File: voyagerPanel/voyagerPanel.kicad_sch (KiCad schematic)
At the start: 22 parts, among them J1 USB_C_Receptacle_USB2.0_16P, J2 Conn_01x02_Pin, U1 ESP32-S3-MINI-1, U2 MCP1700x-330xxMB, U4 TP4056-42-ESOP8

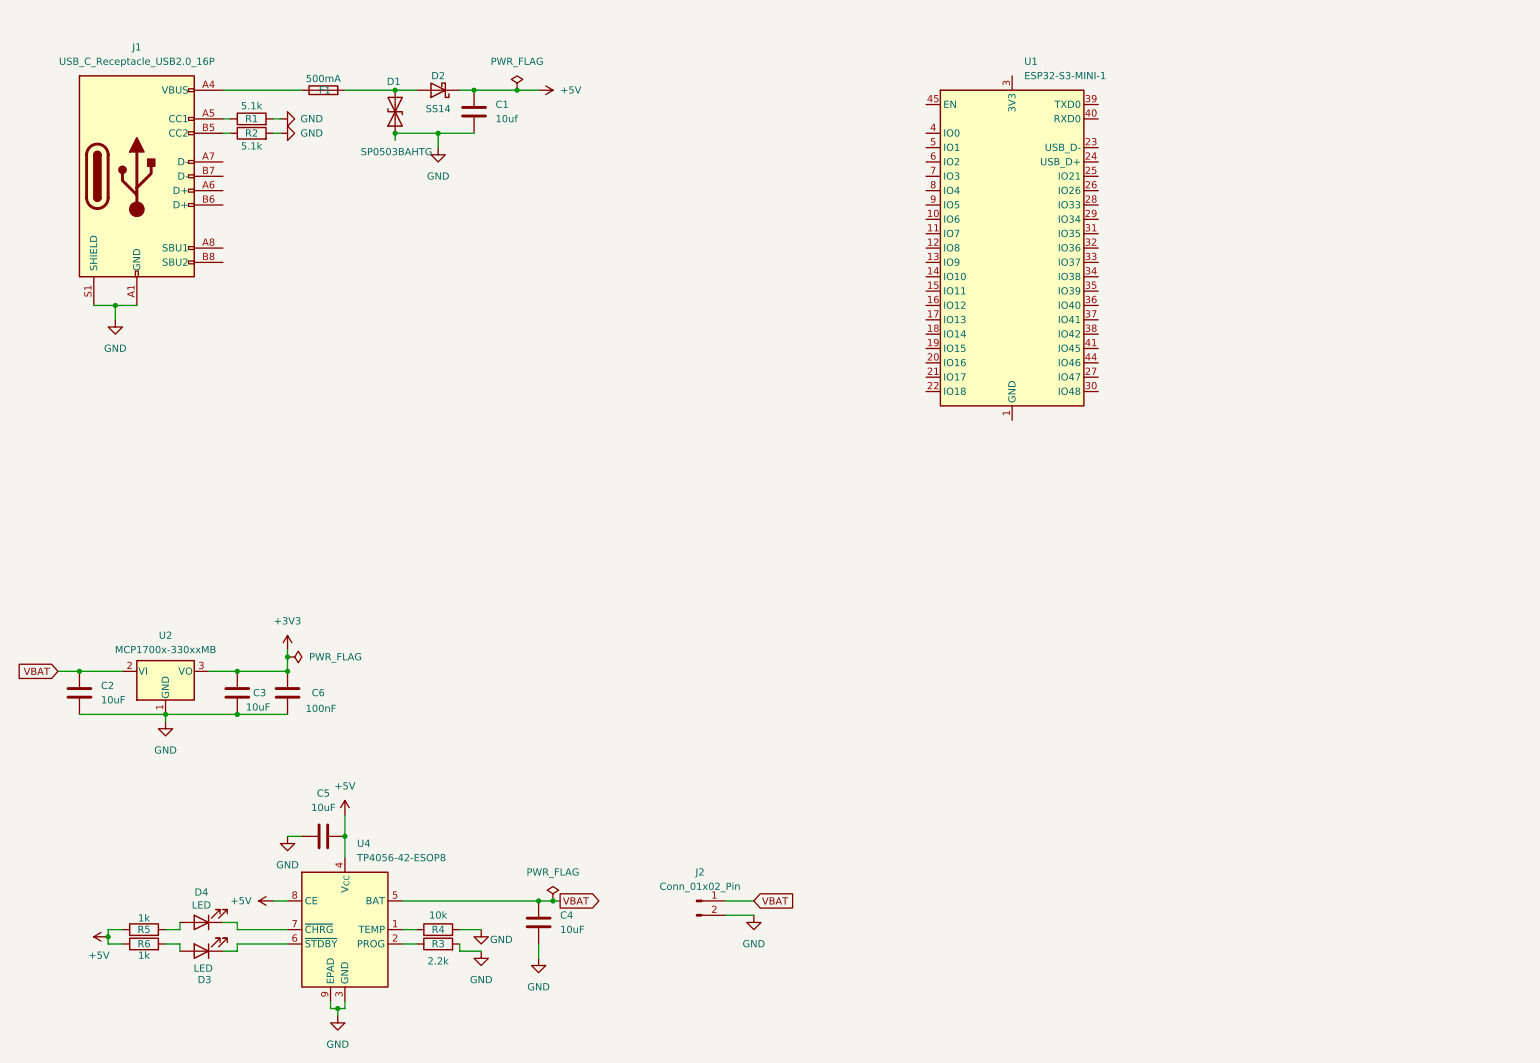
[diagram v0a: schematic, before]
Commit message: Finished schematic creating pcb
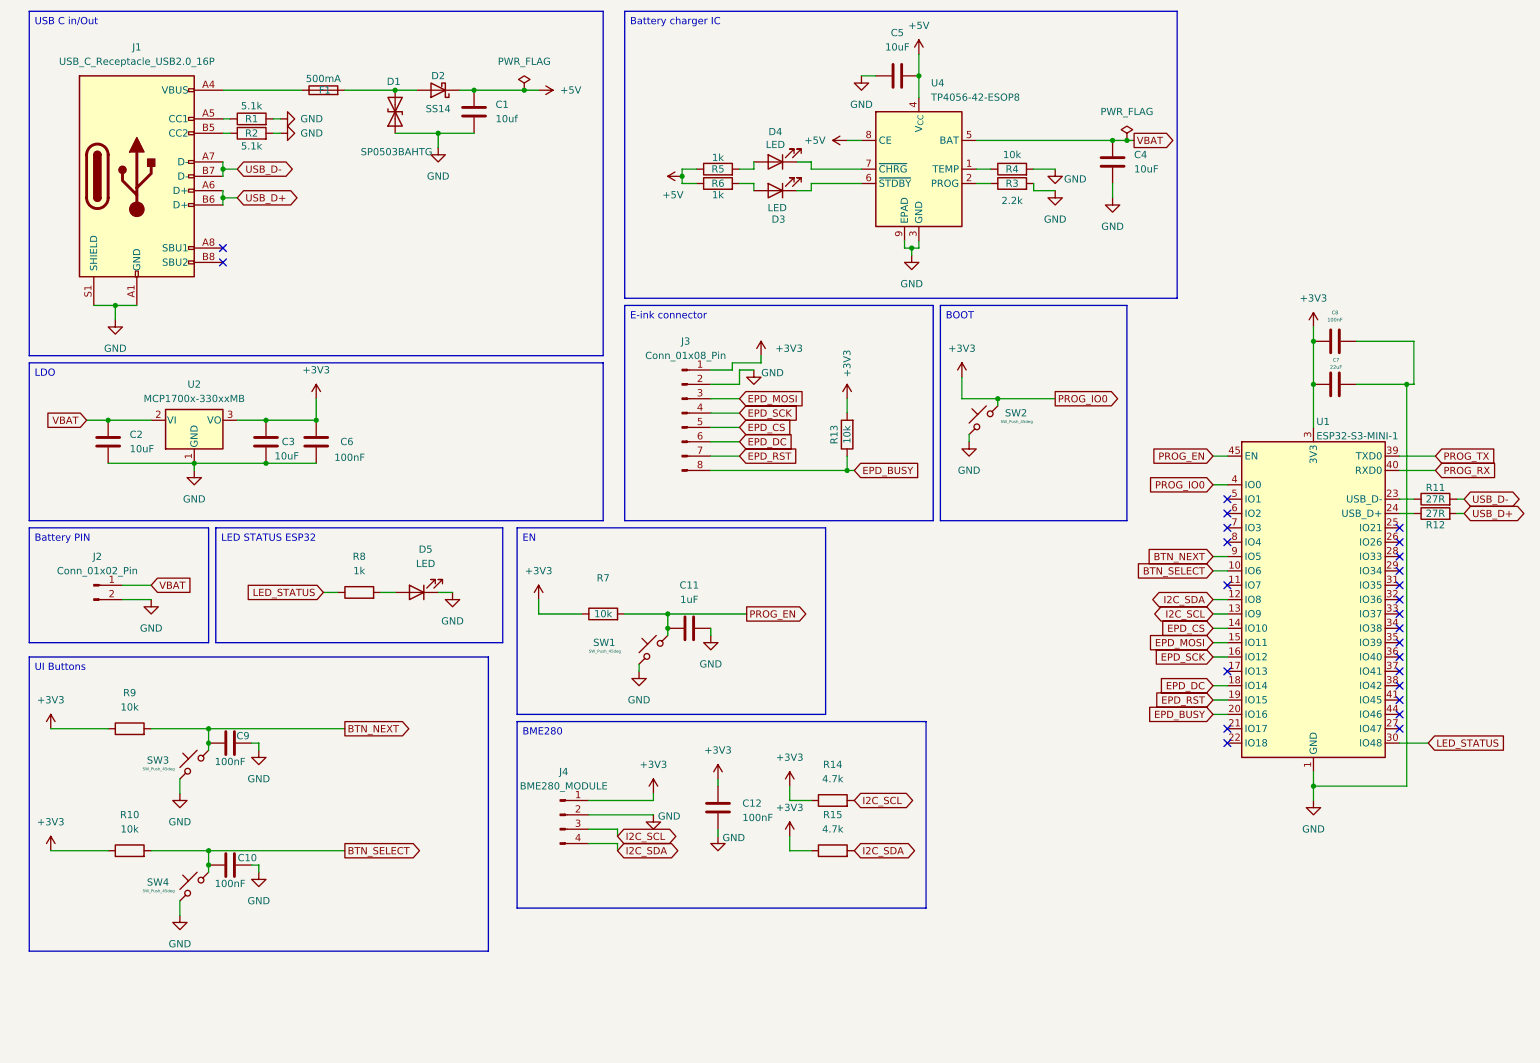
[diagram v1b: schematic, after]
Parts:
- added C10, C12, C8, C9: 100nF, Capacitor_SMD:C_0805_2012Metric, symbol Device:C
- added C11: 1uF, Capacitor_SMD:C_0805_2012Metric, symbol Device:C
- added C7: 22uF, Capacitor_SMD:C_0805_2012Metric, symbol Device:C
- added D5: LED, LED_SMD:LED_0805_2012Metric, symbol Device:LED
- added J3: Conn_01x08_Pin, Connector_PinHeader_2.54mm:PinHeader_1x08_P2.54mm_Vertical, symbol Connector:Conn_01x08_Pin
- added J4: BME280_MODULE, Connector_PinHeader_2.54mm:PinHeader_1x04_P2.54mm_Vertical, symbol Connector:Conn_01x04_Pin
- added R10, R13, R7, R9: 10k, Resistor_SMD:R_0805_2012Metric, symbol Device:R
- added R11, R12: 27R, Resistor_SMD:R_0805_2012Metric, symbol Device:R
- added R14, R15: 4.7k, Resistor_SMD:R_0805_2012Metric, symbol Device:R
- added R8: 1k, Resistor_SMD:R_0805_2012Metric, symbol Device:R
- added SW1, SW2, SW3, SW4: SW_Push_45deg, Button_Switch_SMD:SW_SPST_TL3342, symbol Switch:SW_Push_45deg
- C1, C2, C3, C4, C5, C6: footprint (none) -> Capacitor_SMD:C_0805_2012Metric
- D1: footprint (none) -> Package_TO_SOT_SMD:SOT-363_SC-70-6
- D3, D4: footprint (none) -> LED_SMD:LED_0805_2012Metric
- F1: footprint (none) -> Fuse:Fuse_1206_3216Metric
- J1: footprint (none) -> Connector_USB:USB_C_Receptacle_HRO_TYPE-C-31-M-12
- J2: footprint (none) -> Connector_JST:JST_PH_B2B-PH-K_1x02_P2.00mm_Vertical
- R1, R2, R3, R4, R5, R6: footprint (none) -> Resistor_SMD:R_0805_2012Metric
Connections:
- net +3V3: now also U1.3 (3V3), U1.4 (IO0), C12.1, C7.1, C8.1, J3.1 (Pin_1), J4.1 (Pin_1), R10.1, R13.2, R14.1, R15.1, R7.1, R9.1, SW2.2
- net GND: now also U1.1 (GND), U1.2 (GND), U1.42 (GND), U1.43 (GND), U1.46 (GND), U1.47 (GND), U1.48 (GND), U1.49 (GND), U1.50 (GND), U1.51 (GND), U1.52 (GND), U1.53 (GND), U1.54 (GND), U1.55 (GND), U1.56 (GND), U1.57 (GND), U1.58 (GND), U1.59 (GND), U1.60 (GND), U1.61 (GND), U1.62 (GND), U1.63 (GND), U1.64 (GND), U1.65 (GND), C10.2, C11.1, C12.2, C7.2, C8.2, C9.2, D5.1 (K), J3.2 (Pin_2), J4.2 (Pin_2), SW1.1, SW2.1, SW3.1, SW4.1
- net BTN_SELECT: now reaches U1.10 (IO6)
- net BTN_SELECT: now also C10.1, R10.2, SW4.2
- net I2C_SDA: now reaches U1.12 (IO8)
- net I2C_SDA: now also J4.4 (Pin_4), R15.2
- net I2C_SCL: now reaches U1.13 (IO9)
- net I2C_SCL: now also J4.3 (Pin_3), R14.2
- net EPD_CS: now reaches U1.14 (IO10)
- net EPD_CS: now also J3.5 (Pin_5)
- net EPD_MOSI: now reaches U1.15 (IO11)
- net EPD_MOSI: now also J3.3 (Pin_3)
- net EPD_SCK: now reaches U1.16 (IO12)
- net EPD_SCK: now also J3.4 (Pin_4)
- net EPD_DC: now reaches U1.18 (IO14)
- net EPD_DC: now also J3.6 (Pin_6)
- net EPD_RST: now reaches U1.19 (IO15)
- net EPD_RST: now also J3.7 (Pin_7)
- net EPD_BUSY: now reaches U1.20 (IO16)
- net EPD_BUSY: now also J3.8 (Pin_8), R13.1
- net at U1.23 (USB_D-): now also R11.1
- net at U1.24 (USB_D+): now also R12.1
- net LED_STATUS: now reaches U1.30 (IO48)
- net LED_STATUS: now also R8.1
- net PROG_TX: now reaches U1.39 (TXD0)
- net PROG_RX: now reaches U1.40 (RXD0)
- net PROG_EN: now reaches U1.45 (EN)
- net PROG_EN: now also C11.2, R7.2, SW1.2
- net BTN_NEXT: now reaches U1.9 (IO5)
- net BTN_NEXT: now also C9.1, R9.2, SW3.2
- net USB_D+: now reaches J1.A6 (D+)
- net USB_D+: now also J1.B6 (D+), R12.2
- net USB_D-: now reaches J1.A7 (D-)
- net USB_D-: now also J1.B7 (D-), R11.2
- new net: D5.2 (A), R8.2
- no-connect marks 0 -> 25
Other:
- moved on the sheet: C2, C3, C4, C5, C6, D3, D4, J2, R3, R4, R5, R6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

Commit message: PCB almost finished end of day 2
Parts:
- J2: value Conn_01x02_Pin -> Battery Pin
- J3: value Conn_01x08_Pin -> E-ink
- renumbered R9 to BTNNEXT1, R10 to BTNSELECT1, R7 to EN1, R14 to I2CSCL1, R15 to I2CSDA1, R1 to RC1, R2 to RC2, R8 to RLED1, R13 to e-ink1, R11 to usb1, R12 to usb2
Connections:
- net +3V3: now also SW2.1; no longer SW2.2, U1.4 (IO0)
- net GND: no longer SW2.1
- new net PROG_IO0: SW2.2, U1.4 (IO0)
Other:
- moved on the sheet: SW2
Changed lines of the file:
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@@
 	)
 	(junction
-		(at 189.23 86.36)
-		(diameter 0)
-		(color 0 0 0 0)
-	)
-	(junction
 		(at 31.75 90.17)
 		(diameter 0)
@@
 	(wire
 		(pts
-			(xy 189.23 86.36) (xy 199.39 86.36)
+			(xy 59.69 97.79) (xy 68.58 97.79)
 		)
 		(stroke
@@
 	(wire
 		(pts
-			(xy 59.69 97.79) (xy 68.58 97.79)
+			(xy 186.69 85.09) (xy 182.88 85.09)
 		)
 		(stroke
@@
 	(wire
 		(pts
-			(xy 58.42 168.91) (xy 57.15 168.91)
+			(xy 182.88 85.09) (xy 182.88 82.55)
 		)
 		(stroke
@@
 	(wire
 		(pts
-			(xy 142.24 80.01) (xy 147.32 80.01)
+			(xy 58.42 168.91) (xy 57.15 168.91)
 		)
 		(stroke
@@
 	(wire
 		(pts
-			(xy 44.45 177.8) (xy 44.45 175.26)
+			(xy 142.24 80.01) (xy 147.32 80.01)
 		)
 		(stroke
@@
 	(wire
 		(pts
-			(xy 34.29 119.38) (xy 39.37 119.38)
+			(xy 44.45 177.8) (xy 44.45 175.26)
 		)
 		(stroke
@@
 	(wire
 		(pts
-			(xy 128.27 157.48) (xy 128.27 156.21)
+			(xy 34.29 119.38) (xy 39.37 119.38)
 		)
 		(stroke
@@
 	(wire
 		(pts
-			(xy 213.36 40.64) (xy 212.09 40.64)
+			(xy 128.27 157.48) (xy 128.27 156.21)
 		)
 		(stroke
@@
 	(wire
 		(pts
-			(xy 261.62 83.82) (xy 261.62 154.94)
+			(xy 213.36 40.64) (xy 212.09 40.64)
 		)
 		(stroke
@@
 	(wire
 		(pts
-			(xy 189.23 87.63) (xy 189.23 86.36)
+			(xy 261.62 83.82) (xy 261.62 154.94)
 		)
 		(stroke
@@
 	(wire
 		(pts
-			(xy 182.88 82.55) (xy 182.88 86.36)
-		)
-		(stroke
-			(width 0)
-			(type default)
-		)
-	)
-	(wire
-		(pts
 			(xy 195.58 49.53) (xy 195.58 48.26)
 		)
@@
 	(wire
 		(pts
-			(xy 182.88 86.36) (xy 189.23 86.36)
-		)
-		(stroke
-			(width 0)
-			(type default)
-		)
-	)
-	(wire
-		(pts
 			(xy 227.33 127) (xy 229.87 127)
 		)
@@
 	(wire
 		(pts
+			(xy 199.39 80.01) (xy 199.39 86.36)
+		)
+		(stroke
+			(width 0)
+			(type default)
+		)
+	)
+	(wire
+		(pts
 			(xy 31.75 90.17) (xy 39.37 90.17)
 		)
@@
 	(wire
 		(pts
-			(xy 52.07 49.53) (xy 52.07 50.8)
+			(xy 191.77 80.01) (xy 199.39 80.01)
 		)
 		(stroke
@@
 	(wire
 		(pts
-			(xy 227.33 129.54) (xy 229.87 129.54)
+			(xy 52.07 49.53) (xy 52.07 50.8)
 		)
 		(stroke
@@
 	(wire
 		(pts
-			(xy 260.35 147.32) (xy 265.43 147.32)
+			(xy 227.33 129.54) (xy 229.87 129.54)
 		)
 		(stroke
@@
 	(wire
 		(pts
-			(xy 153.67 49.53) (xy 156.21 49.53)
+			(xy 260.35 147.32) (xy 265.43 147.32)
 		)
 		(stroke
@@
 	(wire
 		(pts
-			(xy 49.53 144.78) (xy 73.66 144.78)
+			(xy 153.67 49.53) (xy 156.21 49.53)
 		)
 		(stroke
@@
 	(wire
 		(pts
-			(xy 21.59 166.37) (xy 31.75 166.37)
+			(xy 49.53 144.78) (xy 73.66 144.78)
 		)
 		(stroke
@@
 	(wire
 		(pts
-			(xy 184.15 92.71) (xy 184.15 93.98)
+			(xy 21.59 166.37) (xy 31.75 166.37)
 		)
 		(stroke
@@
 		(dnp no)
 		(fields_autoplaced yes)
-		(property "Reference" "R14"
+		(property "Reference" "I2CSCL1"
 			(at 160.02 151.13 90)
 			(effects
@@
 			(project ""
 				(path "/900137c4-bd1a-4df5-8116-d18ee50480ac"
-					(reference "R14")
+					(reference "I2CSCL1")
 					(unit 1)
 				)
@@
 	)
 	(symbol
-		(lib_id "power:GND")
-		(at 184.15 93.98 0)
-		(unit 1)
-		(exclude_from_sim no)
-		(in_bom yes)
-		(on_board yes)
-		(dnp no)
-		(fields_autoplaced yes)
-		(property "Reference" "#PWR022"
-			(at 184.15 100.33 0)
-			(effects
-				(font
-					(size 1.27 1.27)
-				)
-				(hide yes)
-			)
-		)
-		(property "Value" "GND"
-			(at 184.15 99.06 0)
-			(effects
-				(font
-					(size 1.27 1.27)
-				)
-			)
-		)
-		(property "Footprint" ""
-			(at 184.15 93.98 0)
-			(effects
-				(font
-					(size 1.27 1.27)
-				)
-				(hide yes)
-			)
-		)
-		(property "Datasheet" ""
-			(at 184.15 93.98 0)
-			(effects
-				(font
-					(size 1.27 1.27)
-				)
-				(hide yes)
-			)
-		)
-		(property "Description" "Power symbol creates a global label with name \"GND\" , ground"
-			(at 184.15 93.98 0)
-			(effects
-				(font
-					(size 1.27 1.27)
-				)
-				(hide yes)
-			)
-		)
-		(pin "1"
-		)
-		(instances
-			(project "voyagerPanel"
-				(path "/900137c4-bd1a-4df5-8116-d18ee50480ac"
-					(reference "#PWR022")
-					(unit 1)
-				)
-			)
-		)
-	)
-	(symbol
 		(lib_id "Battery_Management:TP4056-42-ESOP8")
 		(at 175.26 45.72 0)
@@
 		(dnp no)
 		(fields_autoplaced yes)
-		(property "Reference" "R15"
+		(property "Reference" "I2CSDA1"
 			(at 160.02 160.02 90)
 			(effects
@@
 			(project "voyagerPanel"
 				(path "/900137c4-bd1a-4df5-8116-d18ee50480ac"
-					(reference "R15")
+					(reference "I2CSDA1")
 					(unit 1)
 				)
@@
 		(on_board yes)
 		(dnp no)
-		(property "Reference" "R2"
+		(property "Reference" "RC2"
 			(at 57.15 39.37 90)
 			(effects
@@
 			(project "voyagerPanel"
 				(path "/900137c4-bd1a-4df5-8116-d18ee50480ac"
-					(reference "R2")
+					(reference "RC2")
 					(unit 1)
 				)
@@
 		(dnp no)
 		(fields_autoplaced yes)
-		(property "Reference" "R9"
+		(property "Reference" "BTNNEXT1"
 			(at 35.56 138.43 90)
 			(effects
@@
 			(project ""
 				(path "/900137c4-bd1a-4df5-8116-d18ee50480ac"
-					(reference "R9")
+					(reference "BTNNEXT1")
 					(unit 1)
 				)
@@
 		(on_board yes)
 		(dnp no)
-		(property "Reference" "R1"
+		(property "Reference" "RC1"
 			(at 57.15 36.83 90)
 			(effects
@@
 			(project ""
 				(path "/900137c4-bd1a-4df5-8116-d18ee50480ac"
-					(reference "R1")
+					(reference "RC1")
 					(unit 1)
 				)
@@
 			)
 		)
-		(property "Value" "Conn_01x08_Pin"
+		(property "Value" "E-ink"
 			(at 133.985 78.74 0)
 			(effects
@@
 		(on_board yes)
 		(dnp no)
-		(property "Reference" "R13"
+		(property "Reference" "e-ink1"
 			(at 160.274 92.71 90)
 			(effects
@@
 			(project ""
 				(path "/900137c4-bd1a-4df5-8116-d18ee50480ac"
-					(reference "R13")
+					(reference "e-ink1")
 					(unit 1)
 				)
@@
 		(dnp no)
 		(fields_autoplaced yes)
-		(property "Reference" "R8"
+		(property "Reference" "RLED1"
 			(at 76.2 114.3 90)
 			(effects
@@
 			(project ""
 				(path "/900137c4-bd1a-4df5-8116-d18ee50480ac"
-					(reference "R8")
+					(reference "RLED1")
 					(unit 1)
 				)
@@
 		(on_board yes)
 		(dnp no)
-		(property "Reference" "R7"
+		(property "Reference" "EN1"
 			(at 119.38 118.11 90)
 			(effects
@@
 			(project ""
 				(path "/900137c4-bd1a-4df5-8116-d18ee50480ac"
-					(reference "R7")
+					(reference "EN1")
 					(unit 1)
 				)
@@
 			)
 		)
-		(property "Value" "Conn_01x02_Pin"
+		(property "Value" "Battery Pin"
 			(at 29.845 116.84 0)
 			(effects
@@
 	(symbol
 		(lib_id "Switch:SW_Push_45deg")
-		(at 186.69 90.17 90)
+		(at 189.23 82.55 90)
 		(unit 1)
 		(exclude_from_sim no)
@@
 		(dnp no)
 		(property "Reference" "SW2"
-			(at 190.5 88.8999 90)
+			(at 193.04 81.2799 90)
 			(effects
 				(font
@@
 		)
 		(property "Value" "SW_Push_45deg"
-			(at 189.738 90.424 90)
+			(at 192.278 82.804 90)
 			(effects
 				(font
@@
 		)
 		(property "Footprint" "Button_Switch_SMD:SW_SPST_TL3342"
-			(at 186.69 90.17 0)
+			(at 189.23 82.55 0)
 			(effects
 				(font
@@
 		)
 		(property "Datasheet" "~"
-			(at 186.69 90.17 0)
+			(at 189.23 82.55 0)
 			(effects
 				(font
@@
 		)
 		(property "Description" "Push button switch, normally open, two pins, 45° tilted"
-			(at 186.69 90.17 0)
+			(at 189.23 82.55 0)
 			(effects
 				(font
@@
 		(on_board yes)
 		(dnp no)
-		(property "Reference" "R12"
+		(property "Reference" "usb2"
 			(at 266.7 108.712 90)
 			(effects
@@
 			(project "voyagerPanel"
 				(path "/900137c4-bd1a-4df5-8116-d18ee50480ac"
-					(reference "R12")
+					(reference "usb2")
 					(unit 1)
 				)
@@
 		(dnp no)
 		(fields_autoplaced yes)
-		(property "Reference" "R10"
+		(property "Reference" "BTNSELECT1"
 			(at 35.56 160.02 90)
 			(effects
@@
 			(project "voyagerPanel"
 				(path "/900137c4-bd1a-4df5-8116-d18ee50480ac"
-					(reference "R10")
+					(reference "BTNSELECT1")
 					(unit 1)
 				)
@@
 		(on_board yes)
 		(dnp no)
-		(property "Reference" "R11"
+		(property "Reference" "usb1"
 			(at 266.7 102.108 90)
 			(effects
@@
 			(project "voyagerPanel"
 				(path "/900137c4-bd1a-4df5-8116-d18ee50480ac"
-					(reference "R11")
+					(reference "usb1")
 					(unit 1)
 				)

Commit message: finished PCB
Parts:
- renumbered I2CSCL1 to R14, I2CSDA1 to R15
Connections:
- net +3V3: no longer SW2.1
- net GND: now also SW2.1
